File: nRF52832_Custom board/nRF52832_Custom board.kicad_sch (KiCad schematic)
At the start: 32 parts, among them J1 USB_C, J2 Conn_01x02_Pin, SW1 SW_Push, SW2 SW_Push, U1 nRF52832-QFxx, U2 MCP73831-2-OT, U3 AP2112K-3.3, Y1 32MHZ, Y2 32MHZ

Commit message: Foot Prints added
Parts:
- C2: footprint (none) -> Capacitor_SMD:C_1206_3216Metric_Pad1.33x1.80mm_HandSolder
- R5, R6, R7: footprint (none) -> Resistor_SMD:R_1206_3216Metric_Pad1.30x1.75mm_HandSolder
- SW1, SW2: footprint (none) -> Button_Switch_SMD:SW_Tactile_SPST_NO_Straight_CK_PTS636Sx25SMTRLFS
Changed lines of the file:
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@@
 			)
 		)
-		(property "Footprint" ""
+		(property "Footprint" "Button_Switch_SMD:SW_Tactile_SPST_NO_Straight_CK_PTS636Sx25SMTRLFS"
 			(at 255.27 20.32 0)
 			(effects
@@
 			)
 		)
-		(property "Footprint" ""
+		(property "Footprint" "Capacitor_SMD:C_1206_3216Metric_Pad1.33x1.80mm_HandSolder"
 			(at 37.7952 165.1 0)
 			(effects
@@
 			)
 		)
-		(property "Footprint" ""
+		(property "Footprint" "Button_Switch_SMD:SW_Tactile_SPST_NO_Straight_CK_PTS636Sx25SMTRLFS"
 			(at 256.54 34.29 0)
 			(effects
@@
 			)
 		)
-		(property "Footprint" ""
+		(property "Footprint" "Resistor_SMD:R_1206_3216Metric_Pad1.30x1.75mm_HandSolder"
 			(at 273.05 37.592 90)
 			(effects
@@
 			)
 		)
-		(property "Footprint" ""
+		(property "Footprint" "Resistor_SMD:R_1206_3216Metric_Pad1.30x1.75mm_HandSolder"
 			(at 274.32 51.562 90)
 			(effects
@@
 			)
 		)
-		(property "Footprint" ""
+		(property "Footprint" "Resistor_SMD:R_1206_3216Metric_Pad1.30x1.75mm_HandSolder"
 			(at 271.78 23.622 90)
 			(effects

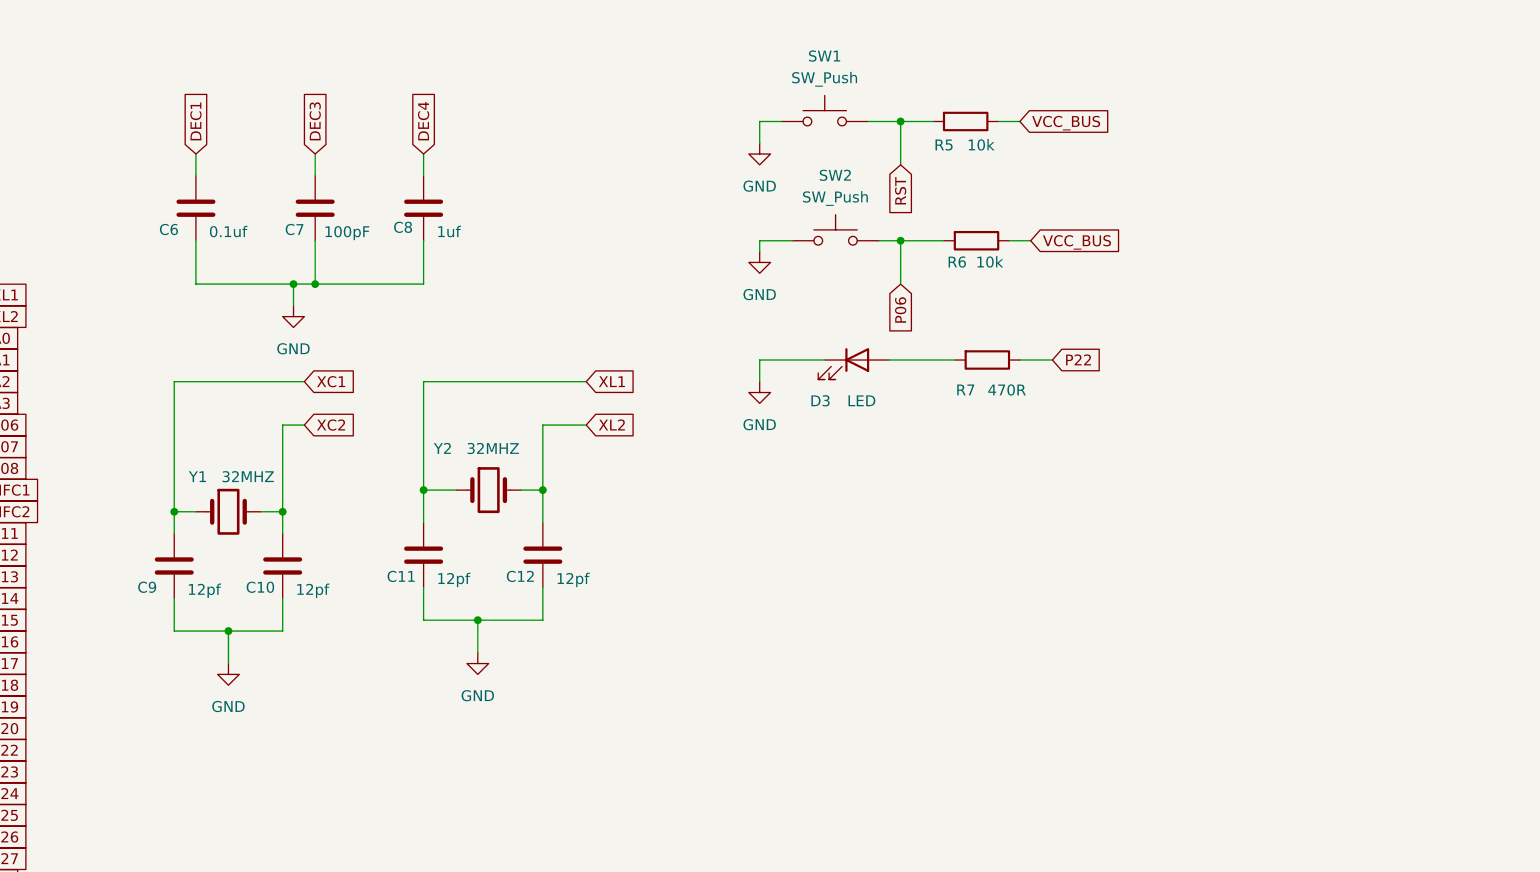
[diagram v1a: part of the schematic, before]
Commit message: Updated after errors in Crystal design
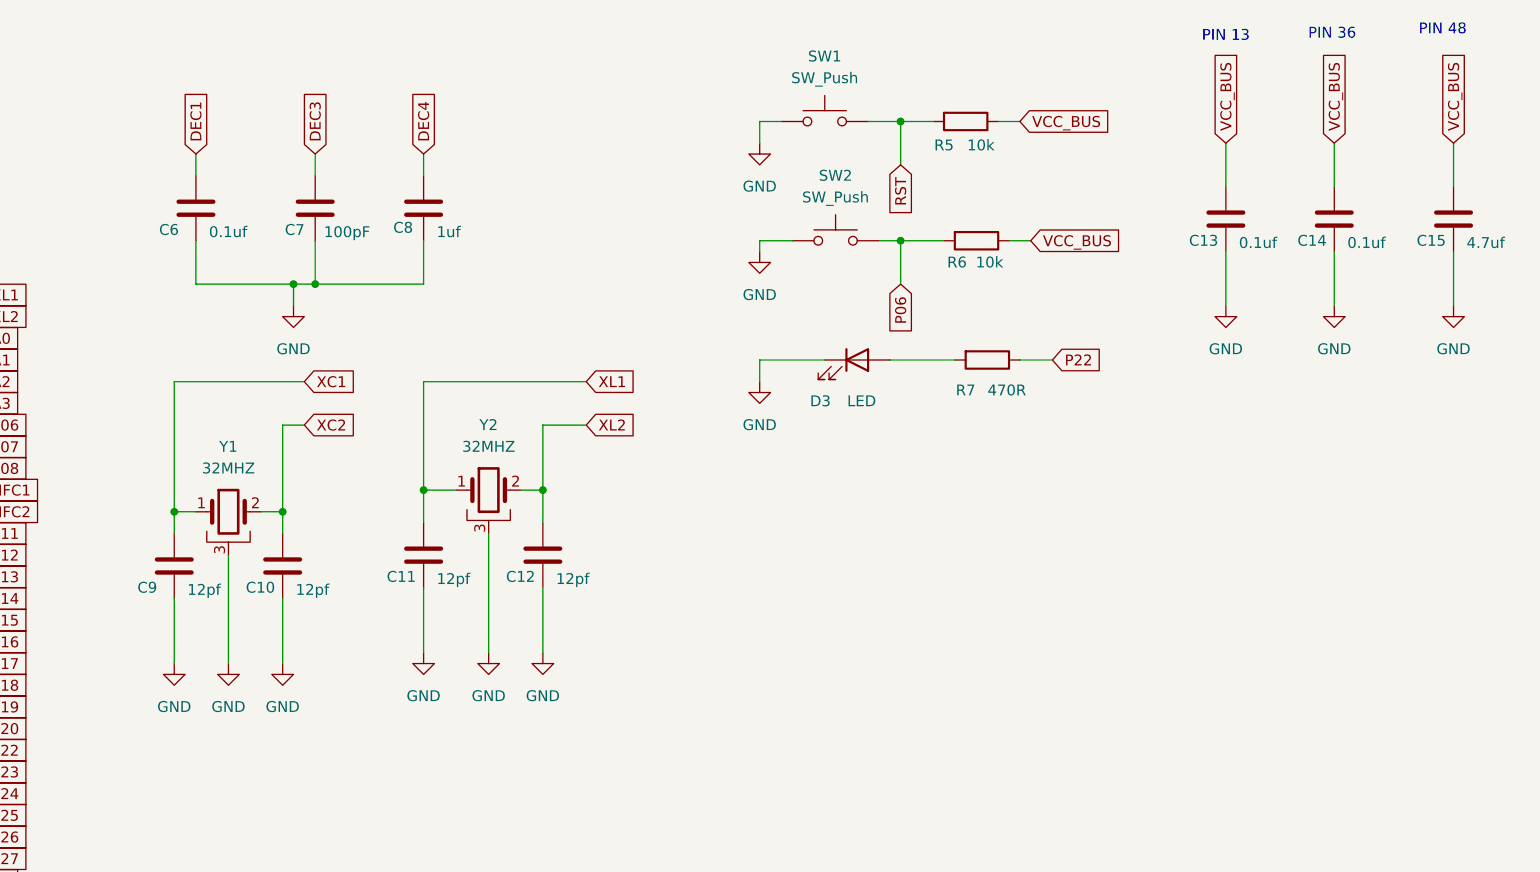
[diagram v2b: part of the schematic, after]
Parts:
- removed Y1, Y2: 32MHZ, Oscillator:Oscillator_SMD_Abracon_ASCO-4Pin_1.6x1.2mm, symbol Device:Crystal
- added C13, C14: 0.1uf, Capacitor_SMD:C_1206_3216Metric_Pad1.33x1.80mm_HandSolder, symbol Device:C
- added C15: 4.7uf, Capacitor_SMD:C_1206_3216Metric_Pad1.33x1.80mm_HandSolder, symbol Device:C
- added Y1, Y2: 32MHZ, symbol Device:Crystal_GND3
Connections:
- net GND: now also C13.2, C14.2, C15.2, Y1.3, Y2.3
- net VCC_BUS: now also C13.1, C14.1, C15.1
- net XC1: now also Y1.1
- net XC2: now also Y1.2
- net XL1: now also Y2.1
- net XL2: now also Y2.2
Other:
- note added: "PIN 13"
- note added: "PIN 36"
- note added: "PIN 48"

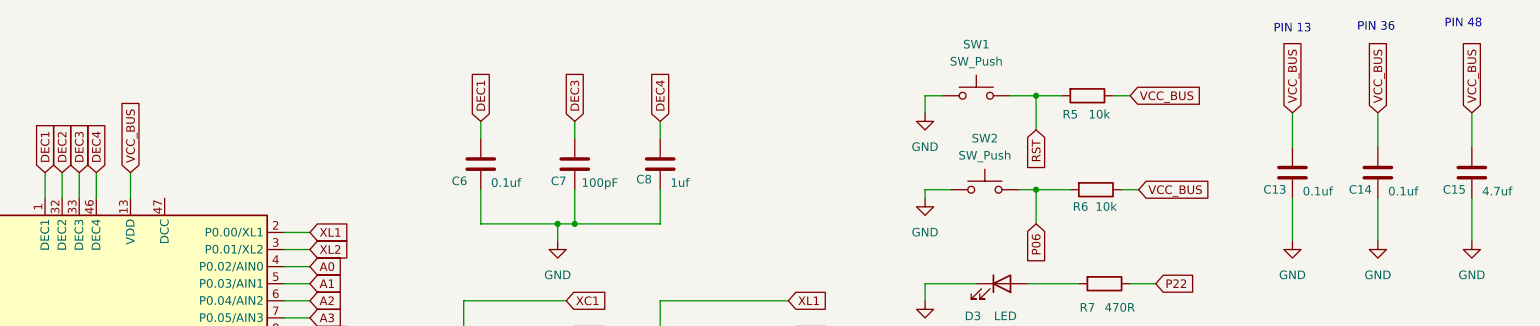
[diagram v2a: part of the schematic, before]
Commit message: VCC error Fixed
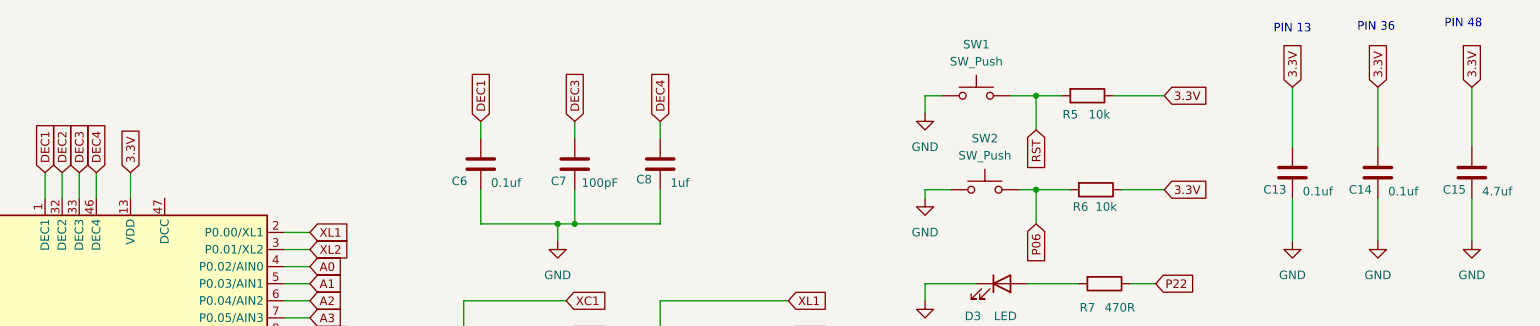
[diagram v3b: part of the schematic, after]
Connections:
- net 3.3V: now also C13.1, C14.1, C15.1, R5.1, R6.1, U1.13 (VDD), U1.36 (VDD), U1.48 (VDD)
- net VCC_BUS: no longer C13.1, C14.1, C15.1, R5.1, R6.1, U1.13 (VDD), U1.36 (VDD), U1.48 (VDD)

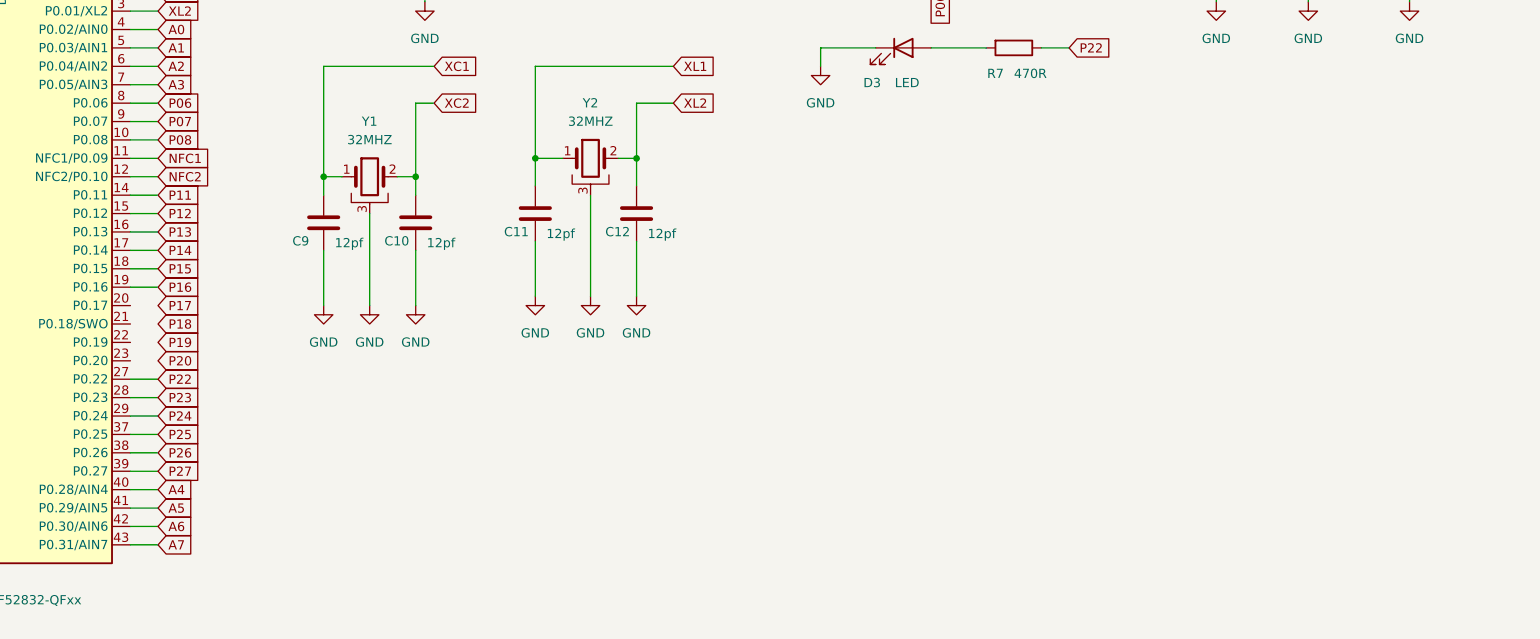
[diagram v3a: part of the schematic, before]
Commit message: JST connetectors added
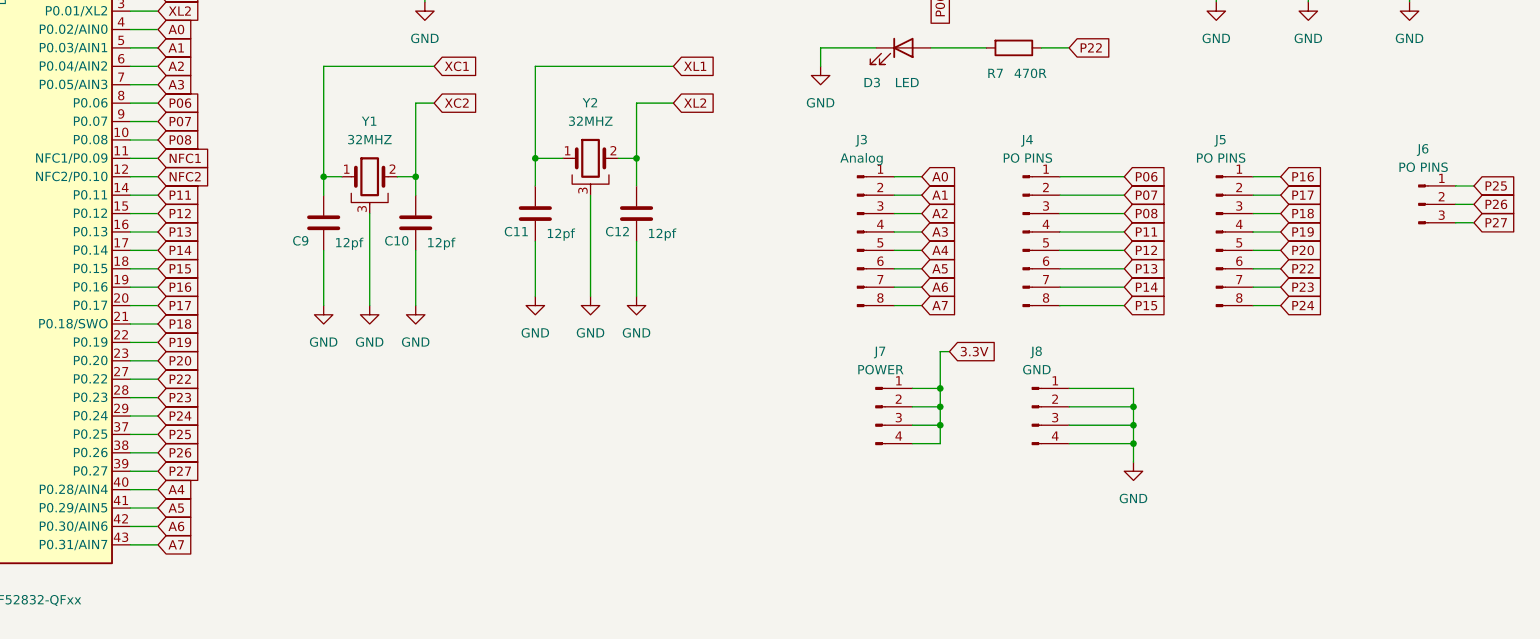
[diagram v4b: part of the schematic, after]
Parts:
- added J3: Analog, Connector_JST:JST_EH_B8B-EH-A_1x08_P2.50mm_Vertical, symbol Connector:Conn_01x08_Pin
- added J4, J5: PO PINS, Connector_JST:JST_EH_B8B-EH-A_1x08_P2.50mm_Vertical, symbol Connector:Conn_01x08_Pin
- added J6: PO PINS, Connector_JST:JST_EH_B3B-EH-A_1x03_P2.50mm_Vertical, symbol Connector:Conn_01x03_Pin
- added J7: POWER, Connector_JST:JST_EH_B4B-EH-A_1x04_P2.50mm_Vertical, symbol Connector:Conn_01x04_Pin
- added J8: GND, Connector_JST:JST_EH_B4B-EH-A_1x04_P2.50mm_Vertical, symbol Connector:Conn_01x04_Pin
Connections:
- net 3.3V: now also J7.1 (Pin_1), J7.2 (Pin_2), J7.3 (Pin_3), J7.4 (Pin_4)
- net A0: now also J3.1 (Pin_1)
- net A1: now also J3.2 (Pin_2)
- net A2: now also J3.3 (Pin_3)
- net A3: now also J3.4 (Pin_4)
- net A4: now also J3.5 (Pin_5)
- net A5: now also J3.6 (Pin_6)
- net A6: now also J3.7 (Pin_7)
- net A7: now also J3.8 (Pin_8)
- net GND: now also J8.1 (Pin_1), J8.2 (Pin_2), J8.3 (Pin_3), J8.4 (Pin_4)
- net P06: now also J4.1 (Pin_1)
- net P07: now also J4.2 (Pin_2)
- net P08: now also J4.3 (Pin_3)
- net P11: now also J4.4 (Pin_4)
- net P12: now also J4.5 (Pin_5)
- net P13: now also J4.6 (Pin_6)
- net P14: now also J4.7 (Pin_7)
- net P15: now also J4.8 (Pin_8)
- net P16: now also J5.1 (Pin_1)
- net P17: now also U1.20 (P0.17), J5.2 (Pin_2)
- net P18: now also U1.21 (P0.18/SWO), J5.3 (Pin_3)
- net P19: now also U1.22 (P0.19), J5.4 (Pin_4)
- net P20: now also U1.23 (P0.20), J5.5 (Pin_5)
- net P22: now also J5.6 (Pin_6)
- net P23: now also J5.7 (Pin_7)
- net P24: now also J5.8 (Pin_8)
- net P25: now also J6.1 (Pin_1)
- net P26: now also J6.2 (Pin_2)
- net P27: now also J6.3 (Pin_3)

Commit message: ERC errors Fixed
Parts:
- removed Y2: 32MHZ, symbol Device:Crystal_GND3
- added AE1: Antenna, RF_Antenna:Texas_SWRA117D_2.4GHz_Right, symbol Device:Antenna
- added C16: DNP, Capacitor_SMD:C_1206_3216Metric_Pad1.33x1.80mm_HandSolder, symbol Device:C
- added C17: 0.8pf, Capacitor_SMD:C_1206_3216Metric_Pad1.33x1.80mm_HandSolder, symbol Device:C
- added J9: Programming, Connector_JST:JST_EH_B4B-EH-A_1x04_P2.50mm_Vertical, symbol Connector:Conn_01x04_Pin
- added L1: 3.9H, Inductor_SMD:L_1206_3216Metric_Pad1.22x1.90mm_HandSolder, symbol Device:L
- added Y2: 32.768KHZ, Crystal:Crystal_SMD_3215-2Pin_3.2x1.5mm, symbol Device:Crystal
- C4, C5: value C -> 10uf
- J2: value Conn_01x02_Pin -> Battery Connector
- Y1: footprint (none) -> Oscillator:Oscillator_SMD_Abracon_ASE-4Pin_3.2x2.5mm_HandSoldering
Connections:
- net 3.3V: now also J9.1 (Pin_1)
- net ANT: now also C17.1, L1.2
- net GND: now also C16.2, C17.2, J9.4 (Pin_4)
- net SWDCLK: now also J9.3 (Pin_3)
- net SWDIO: now also J9.2 (Pin_2)
- net XL1: now also Y2.1
- net XL2: now also Y2.2
- net DEC2: no longer names the net of U1.32 (DEC2)
- net VCC_BUS renamed VBUS
- new net: AE1.1 (A), C16.1, L1.1
- no-connect marks 0 -> 8
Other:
- moved on the sheet: C10, C11, C12, C13, C14, C15, C2, C4, C5, C6, C7, C8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

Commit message: updated
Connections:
- net NFC1: no longer names the net of U1.11 (NFC1/P0.09)
- net NFC2: no longer names the net of U1.12 (NFC2/P0.10)
- no-connect marks 8 -> 10
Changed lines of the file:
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@@
+	)
+	(no_connect
+		(at 275.59 59.69)
 	)
 	(no_connect
@@
 	(no_connect
 		(at 48.26 48.26)
+	)
+	(no_connect
+		(at 275.59 62.23)
 	)
 	(no_connect
@@
 		)
 	)
-	(global_label "NFC2"
-		(shape input)
-		(at 275.59 62.23 0)
+	(global_label "XC1"
+		(shape input)
+		(at 223.52 69.85 180)
+		(fields_autoplaced yes)
+		(effects
+			(font
+				(size 1.27 1.27)
+			)
+			(justify right)
+		)
+		(property "Intersheetrefs" "${INTERSHEET_REFS}"
+			(at 216.8458 69.85 0)
+			(effects
+				(font
+					(size 1.27 1.27)
+				)
+				(justify right)
+				(hide yes)
+			)
+		)
+	)
+	(global_label "P20"
+		(shape input)
+		(at 275.59 87.63 0)
 		(fields_autoplaced yes)
 		(effects
@@
 		)
 		(property "Intersheetrefs" "${INTERSHEET_REFS}"
-			(at 283.4738 62.23 0)
+			(at 282.2642 87.63 0)
 			(effects
 				(font
@@
 		)
 	)
-	(global_label "XC1"
-		(shape input)
-		(at 223.52 69.85 180)
+	(global_label "P06"
+		(shape input)
+		(at 314.96 49.53 270)
 		(fields_autoplaced yes)
 		(effects
@@
 		)
 		(property "Intersheetrefs" "${INTERSHEET_REFS}"
-			(at 216.8458 69.85 0)
+			(at 314.96 56.2042 90)
 			(effects
 				(font
@@
 		)
 	)
-	(global_label "P20"
-		(shape input)
-		(at 275.59 87.63 0)
+	(global_label "3.3V"
+		(shape input)
+		(at 389.89 110.49 0)
 		(fields_autoplaced yes)
 		(effects
@@
 		)
 		(property "Intersheetrefs" "${INTERSHEET_REFS}"
-			(at 282.2642 87.63 0)
+			(at 396.9876 110.49 0)
 			(effects
 				(font
@@
 		)
 	)
-	(global_label "P06"
-		(shape input)
-		(at 314.96 49.53 270)
-		(fields_autoplaced yes)
-		(effects
-			(font
-				(size 1.27 1.27)
-			)
-			(justify right)
-		)
-		(property "Intersheetrefs" "${INTERSHEET_REFS}"
-			(at 314.96 56.2042 90)
-			(effects
-				(font
-					(size 1.27 1.27)
-				)
-				(justify right)
+	(global_label "XL2"
+		(shape input)
+		(at 172.72 66.04 0)
+		(fields_autoplaced yes)
+		(effects
+			(font
+				(size 1.27 1.27)
+			)
+			(justify left)
+		)
+		(property "Intersheetrefs" "${INTERSHEET_REFS}"
+			(at 179.1523 66.04 0)
+			(effects
+				(font
+					(size 1.27 1.27)
+				)
+				(justify left)
+				(hide yes)
+			)
+		)
+	)
+	(global_label "P27"
+		(shape input)
+		(at 388.62 82.55 0)
+		(fields_autoplaced yes)
+		(effects
+			(font
+				(size 1.27 1.27)
+			)
+			(justify left)
+		)
+		(property "Intersheetrefs" "${INTERSHEET_REFS}"
+			(at 395.2942 82.55 0)
+			(effects
+				(font
+					(size 1.27 1.27)
+				)
+				(justify left)
+				(hide yes)
+			)
+		)
+	)
+	(global_label "STAT"
+		(shape input)
+		(at 46.99 109.22 0)
+		(fields_autoplaced yes)
+		(effects
+			(font
+				(size 1.27 1.27)
+			)
+			(justify left)
+		)
+		(property "Intersheetrefs" "${INTERSHEET_REFS}"
+			(at 54.2085 109.22 0)
+			(effects
+				(font
+					(size 1.27 1.27)
+				)
+				(justify left)
 				(hide yes)
 			)
@@
 	(global_label "3.3V"
 		(shape input)
-		(at 389.89 110.49 0)
+		(at 334.01 44.45 0)
 		(fields_autoplaced yes)
 		(effects
@@
 		)
 		(property "Intersheetrefs" "${INTERSHEET_REFS}"
-			(at 396.9876 110.49 0)
+			(at 341.1076 44.45 0)
 			(effects
 				(font
@@
 		)
 	)
-	(global_label "XL2"
-		(shape input)
-		(at 172.72 66.04 0)
+	(global_label "P24"
+		(shape input)
+		(at 361.95 93.98 0)
 		(fields_autoplaced yes)
 		(effects
@@
 		)
 		(property "Intersheetrefs" "${INTERSHEET_REFS}"
-			(at 179.1523 66.04 0)
-			(effects
-				(font
-					(size 1.27 1.27)
-				)
-				(justify left)
-				(hide yes)
-			)
-		)
-	)
-	(global_label "P27"
-		(shape input)
-		(at 388.62 82.55 0)
-		(fields_autoplaced yes)
-		(effects
-			(font
-				(size 1.27 1.27)
-			)
-			(justify left)
-		)
-		(property "Intersheetrefs" "${INTERSHEET_REFS}"
-			(at 395.2942 82.55 0)
-			(effects
-				(font
-					(size 1.27 1.27)
-				)
-				(justify left)
-				(hide yes)
-			)
-		)
-	)
-	(global_label "STAT"
-		(shape input)
-		(at 46.99 109.22 0)
-		(fields_autoplaced yes)
-		(effects
-			(font
-				(size 1.27 1.27)
-			)
-			(justify left)
-		)
-		(property "Intersheetrefs" "${INTERSHEET_REFS}"
-			(at 54.2085 109.22 0)
-			(effects
-				(font
-					(size 1.27 1.27)
-				)
-				(justify left)
-				(hide yes)
-			)
-		)
-	)
-	(global_label "3.3V"
-		(shape input)
-		(at 334.01 44.45 0)
-		(fields_autoplaced yes)
-		(effects
-			(font
-				(size 1.27 1.27)
-			)
-			(justify left)
-		)
-		(property "Intersheetrefs" "${INTERSHEET_REFS}"
-			(at 341.1076 44.45 0)
-			(effects
-				(font
-					(size 1.27 1.27)
-				)
-				(justify left)
-				(hide yes)
-			)
-		)
-	)
-	(global_label "P24"
-		(shape input)
-		(at 361.95 93.98 0)
-		(fields_autoplaced yes)
-		(effects
-			(font
-				(size 1.27 1.27)
-			)
-			(justify left)
-		)
-		(property "Intersheetrefs" "${INTERSHEET_REFS}"
 			(at 368.6242 93.98 0)
 			(effects
 				(font
-					(size 1.27 1.27)
-				)
-				(justify left)
-				(hide yes)
-			)
-		)
-	)
-	(global_label "NFC1"
-		(shape input)
-		(at 275.59 59.69 0)
-		(fields_autoplaced yes)
-		(effects
-			(font
-				(size 1.27 1.27)
-			)
-			(justify left)
-		)
-		(property "Intersheetrefs" "${INTERSHEET_REFS}"
-			(at 283.4738 59.69 0)
-			(effects
-				(font
